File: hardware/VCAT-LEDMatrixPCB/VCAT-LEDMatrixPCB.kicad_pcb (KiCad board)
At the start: 2 copper layers, 181 parts, among them IC4 AP64501QSP-13, J1 Conn_01x03

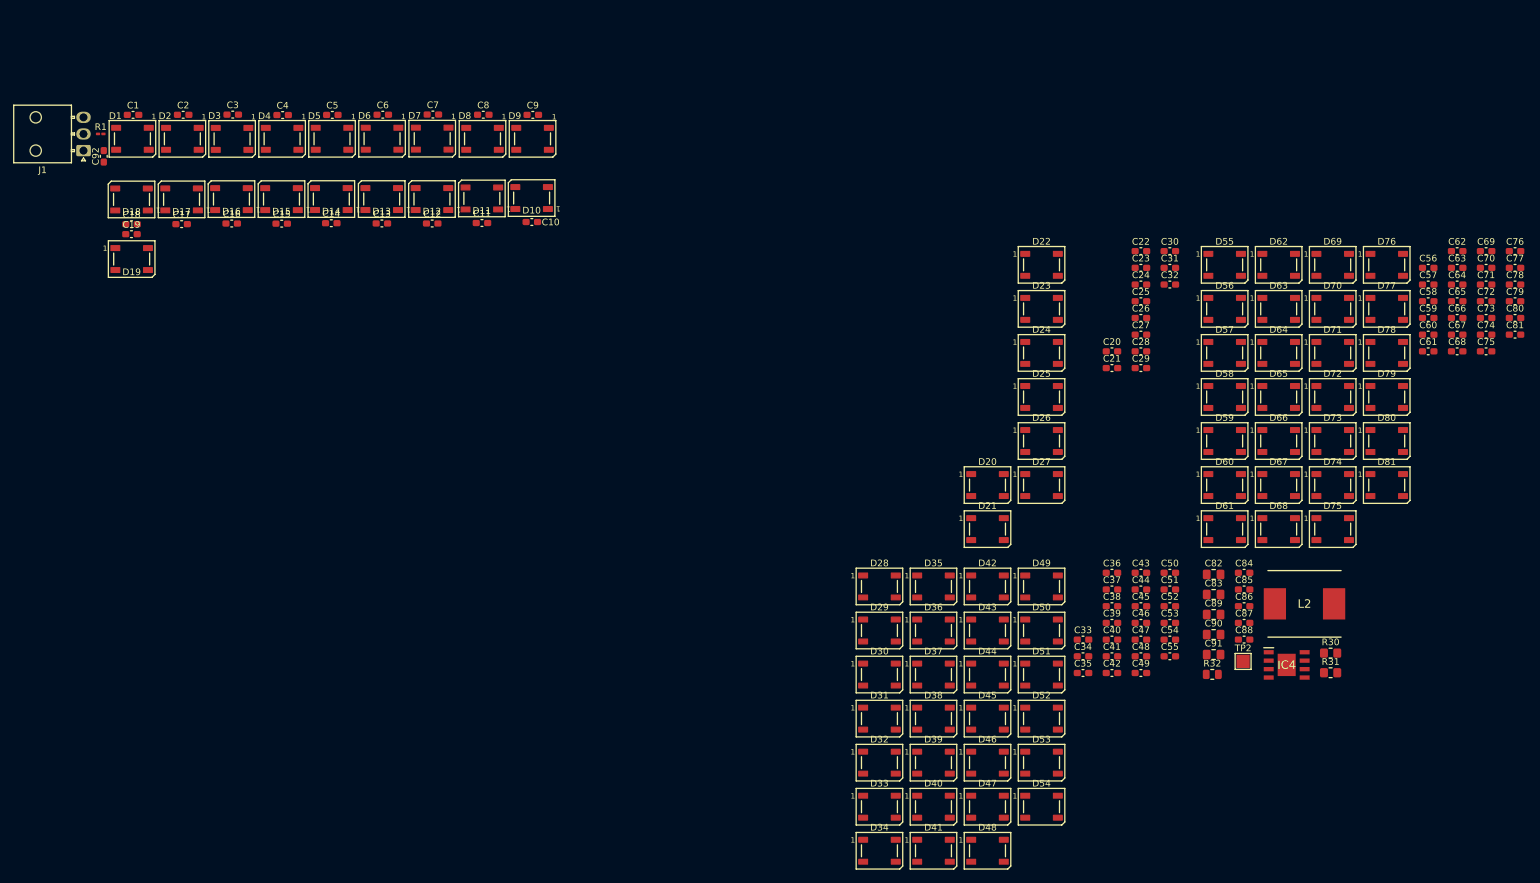
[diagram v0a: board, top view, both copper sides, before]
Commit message: Layout 50% done
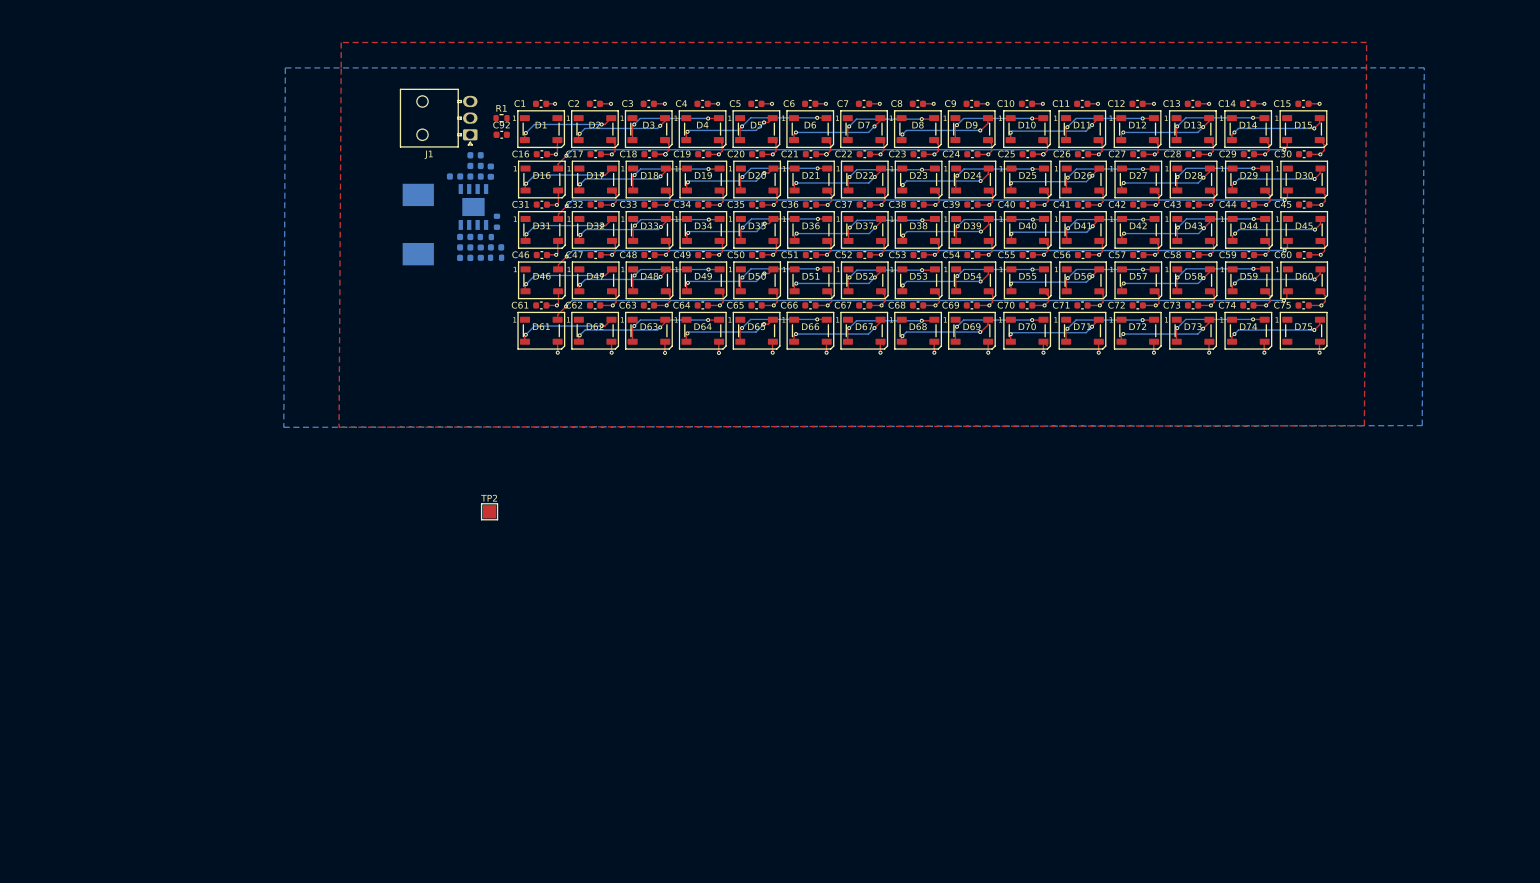
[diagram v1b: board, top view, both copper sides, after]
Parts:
- removed C76, C77, C78, C79, C80, C81: 0.1uF, Capacitor_SMD:C_0603_1608Metric_Pad1.08x0.95mm_HandSolder
- removed D76, D77, D78, D79, D80, D81: WS2812B, LED_SMD:LED_WS2812B_PLCC4_5.0x5.0mm_P3.2mm
- C1, C10, C11, C12, C13, C14, C15, C16, C17, C18, C19, C2, C20, C21, C22, C23, C24, C25, C26, C27, C28, C29, C3, C30, C31, C32, C33, C34, C35, C36, C37, C38, C39, C4, C40, C41, C42, C43, C44, C45, C46, C47, C48, C49, C5, C50, C51, C52, C53, C54, C55, C56, C57, C58, C59, C6, C60, C61, C62, C63, C64, C65, C66, C67, C68, C69, C7, C70, C71, C72, C73, C74, C75, C8, C9, C92: footprint Capacitor_SMD:C_0603_1608Metric_Pad1.08x0.95mm_HandSolder -> Capacitor_SMD:C_0603_1608Metric
- C82, C83, C89, C90, C91: footprint Capacitor_SMD:C_0805_2012Metric_Pad1.18x1.45mm_HandSolder -> Capacitor_SMD:C_0603_1608Metric; moved to B.Cu
- C84, C85, C86, C87, C88: footprint Capacitor_SMD:C_0603_1608Metric_Pad1.08x0.95mm_HandSolder -> Capacitor_SMD:C_0603_1608Metric; moved to B.Cu
- IC4, L2: moved to B.Cu
- R1: footprint Resistor_SMD:R_0201_0603Metric_Pad0.64x0.40mm_HandSolder -> Resistor_SMD:R_0603_1608Metric
- R30, R31: footprint Resistor_SMD:R_0805_2012Metric_Pad1.20x1.40mm_HandSolder -> Resistor_SMD:R_0603_1608Metric; moved to B.Cu
- R32: footprint Resistor_SMD:R_0805_2012Metric -> Resistor_SMD:R_0603_1608Metric; moved to B.Cu
- moved C15 154.6 mm to (209.4, 25.5)
- moved D15 154.0 mm to (209.4, 29.3), turned to 0 degrees
- moved L2 144.9 mm to (76.3, 43.6), turned to -90 degrees
- moved R31 142.9 mm to (86.5, 45.5)
- moved IC4 140.3 mm to (84.6, 41.0), turned to -90 degrees
- moved C14 139.0 mm to (201.1, 25.5)
- moved R30 138.8 mm to (88.0, 48.6), turned to 180 degrees
- moved D14 138.2 mm to (201.1, 29.3), turned to 0 degrees
- moved C86 135.0 mm to (81.9, 36.4), turned to 180 degrees
- moved C61 133.5 mm to (94.8, 55.8)
- moved C84 131.4 mm to (84.9, 33.2)
- moved C62 129.8 mm to (102.9, 55.8)
- moved C85 129.5 mm to (87.2, 35.7), turned to 90 degrees
- moved C83 128.3 mm to (84.9, 34.8)
- moved C87 127.5 mm to (85.7, 47.9), turned to 90 degrees
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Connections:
- C92 pad 2: Net-(J1-Pin_1) -> GND
- J1 pad 1: Net-(J1-Pin_1) -> +24V
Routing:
- net GND: track 0.00 -> 310.3 mm, vias 0 -> 93
- net Net-(D15-DOUT): track 0.00 -> 112.3 mm, vias 0 -> 2
- net Net-(D60-DOUT): track 0.00 -> 112.3 mm, vias 0 -> 2
- net Net-(D45-DOUT): track 0.00 -> 112.3 mm, vias 0 -> 2
- net Net-(D30-DOUT): track 0.00 -> 112.3 mm, vias 0 -> 2
- net Net-(D73-DOUT): track 0.00 -> 15.8 mm, vias 0 -> 2
- net Net-(D13-DOUT): track 0.00 -> 15.8 mm, vias 0 -> 2
- net Net-(D43-DOUT): track 0.00 -> 15.8 mm, vias 0 -> 2
- net Net-(D58-DOUT): track 0.00 -> 15.8 mm, vias 0 -> 2
- net Net-(D28-DOUT): track 0.00 -> 15.8 mm, vias 0 -> 2
- net /Rows4-6/Row7: track 0.00 -> 15.8 mm, vias 0 -> 2
- net Net-(D10-DIN): track 0.00 -> 15.8 mm, vias 0 -> 2
- net Net-(D69-DOUT): track 0.00 -> 15.8 mm, vias 0 -> 2
- net Net-(D39-DOUT): track 0.00 -> 15.8 mm, vias 0 -> 2
- net Net-(D24-DOUT): track 0.00 -> 15.8 mm, vias 0 -> 2
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- added copper zone on F.Cu, net +5V
- added copper zone on B.Cu, net GND

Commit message: Layout Review
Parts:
- added H1: MountingHole, MountingHole:MountingHole_3.2mm_M3, F.Cu at (73.9, 21.5)
- added H2: MountingHole, MountingHole:MountingHole_3.2mm_M3, F.Cu at (210.8, 21.5)
- added H3: MountingHole, MountingHole:MountingHole_3.2mm_M3, F.Cu at (73.9, 68.6)
- added H4: MountingHole, MountingHole:MountingHole_3.2mm_M3, F.Cu at (210.8, 68.6)
- C92, J1: moved to B.Cu
- TP2: footprint TestPoint:TestPoint_Pad_2.0x2.0mm -> TestPoint:TestPoint_Keystone_5005-5009_Compact; moved to B.Cu
- moved TP2 63.0 mm to (82.3, 24.0)
- moved C87 7.25 mm to (90.7, 42.6), turned to -90 degrees
- moved R30 6.81 mm to (88.4, 41.8), turned to 0 degrees
- moved R31 6.50 mm to (92.3, 42.6), turned to 90 degrees
- moved IC4 4.25 mm to (86.7, 37.3)
- moved R32 4.25 mm to (90.2, 39.5)
- moved C82 4.14 mm to (86.8, 32.7)
- moved C83 4.14 mm to (86.8, 31.1)
- moved C84 4.14 mm to (86.8, 29.5)
- moved C85 4.14 mm to (89.1, 32.0)
- moved C88 3.71 mm to (88.4, 43.4), turned to 0 degrees
- moved C90 3.68 mm to (83.9, 43.4)
- moved C89 3.68 mm to (83.8, 41.9)
- moved C91 3.68 mm to (83.8, 45.0)
- moved R1 3.26 mm to (88.6, 30.9)
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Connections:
- D75 pad 2: Net-(D75-DOUT) -> unconnected-(D75-DOUT-Pad2)
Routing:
- net +5V: track 0.00 -> 16.1 mm, vias 0 -> 2
- net Net-(D1-DIN): track 0.00 -> 9.19 mm
- net Net-(IC4-SW): track 0.00 -> 8.98 mm
- net Net-(J1-Pin_2): track 0.00 -> 5.73 mm
- net Net-(IC4-BST): track 0.00 -> 5.69 mm, vias 0 -> 2
- net Net-(IC4-FB): track 0.00 -> 4.57 mm
- net Net-(IC4-COMP): track 0.00 -> 3.68 mm
- net GND: track 310.3 -> 307.8 mm, vias 93 -> 90
- net Net-(IC4-SS): track 0.00 -> 2.04 mm
- net Net-(C87-Pad1): track 0.00 -> 1.48 mm
- added copper zone on B.Cu, net +24V
- added copper zone on B.Cu, net +5V
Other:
- board outline added: 144.3 x 54.6 mm
